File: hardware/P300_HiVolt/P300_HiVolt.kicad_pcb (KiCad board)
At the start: 2 copper layers, 14 parts, among them J1 Conn_01x02, J2 Conn_01x08, J3 Conn_01x06, J4 Conn_01x06, J5 12V, J6 5V, T1 HLK-PM12, T2 HLK-PM05

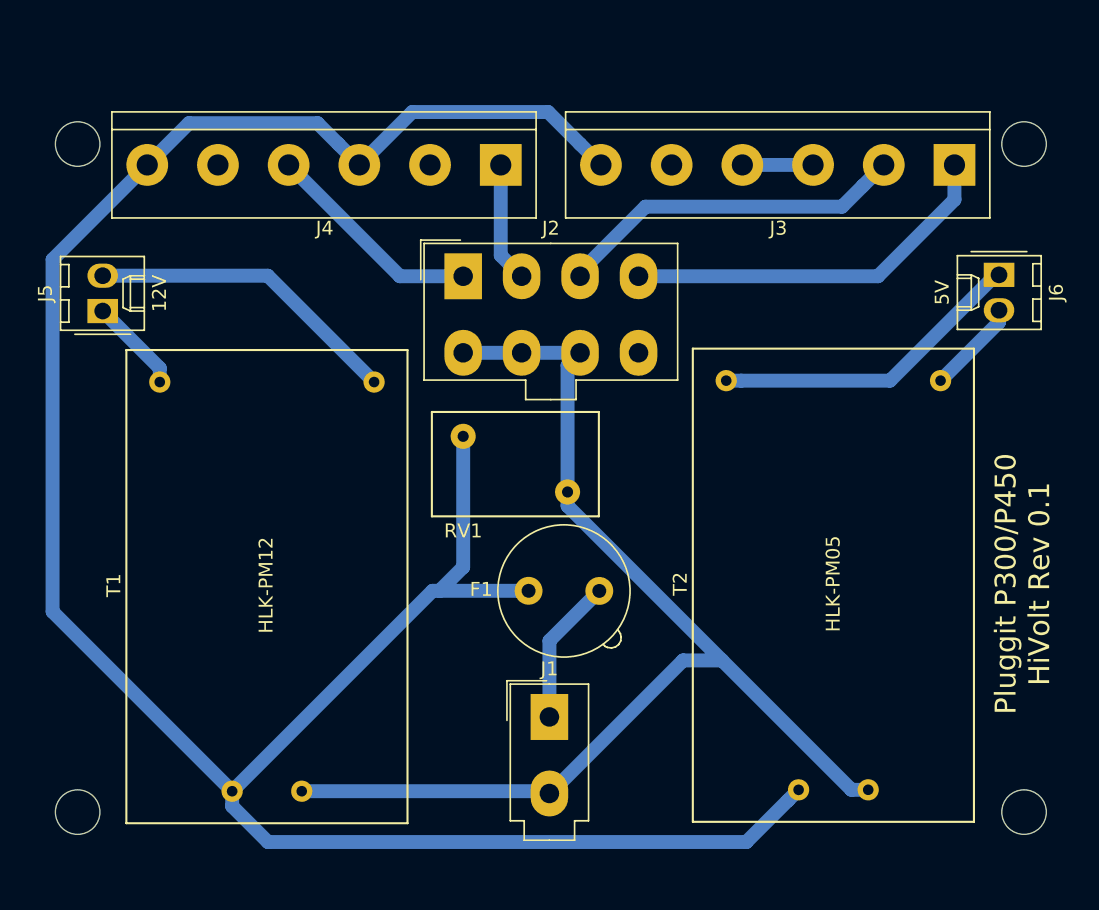
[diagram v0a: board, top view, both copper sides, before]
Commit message: Update der Platinen auf 0.23-dev
Änderungen von 0.22 zu 0.23 - P300_Arduino_IF
 - Linke Seite der Platine vergrößert auf ArduinoMega-Größe
 - Stecker für Displayanschluß ergänzt
 - Fünf weitere Bohrungen für Befestigung ergänzt
 - Leiterbahnen im größeren Abstand zu Durchbohrungen und Bauteilen verlegt
 - Connector für J12 I2C nach links verschoben, damit ausreichend Platz für JTS Stecker
 - Auf dem Stecker J4 sind die beiden Lüfteranschlüsse Lüfter 1 und Lüfter 2 getauscht. Damit ist der Stecker kompatibel zu Pluggit. Der Pluggit-Lüfter-Steuerstecker kann direkt aufgesteckt werden, wenn Molex Stiftleiste - KK - 1x8-polig - Stecker, Molex-Best-Nr. 22272081 verwendet wird.

Änderungen von 0.22 zu 0.23 - P300_HiVolt
 - 230V Lüfteranschluss kompatibel zu Pluggit, Molex Stiftleiste - Mini-Fit Jr - 2x4-polig - Stecker, Molex-Best-Nr. 39281083
 - Stecker J3, J4 für Relais auf Molex Stiftleiste - Mini-Fit Jr - 2x3-polig - Stecker, Molex-Best-Nr. 39288060 geändert.
 - Änderung der Belegung der Stecker J3, J4 für die Verwendung es Relaisboards mit den Ralaisanschlüssen: Mitte = Stromzuführung, links = Nicht geschaltet, rechts geschaltet
 - Räumliche Trennung von 230V und Niedervoltspannungen auf der Platine
 
Neu 0.23 - P300_Display_IF
 - Platine zum Aufstecken des Displays für die räumlich getrennte Montage von Display zu P300_Arduino_IF
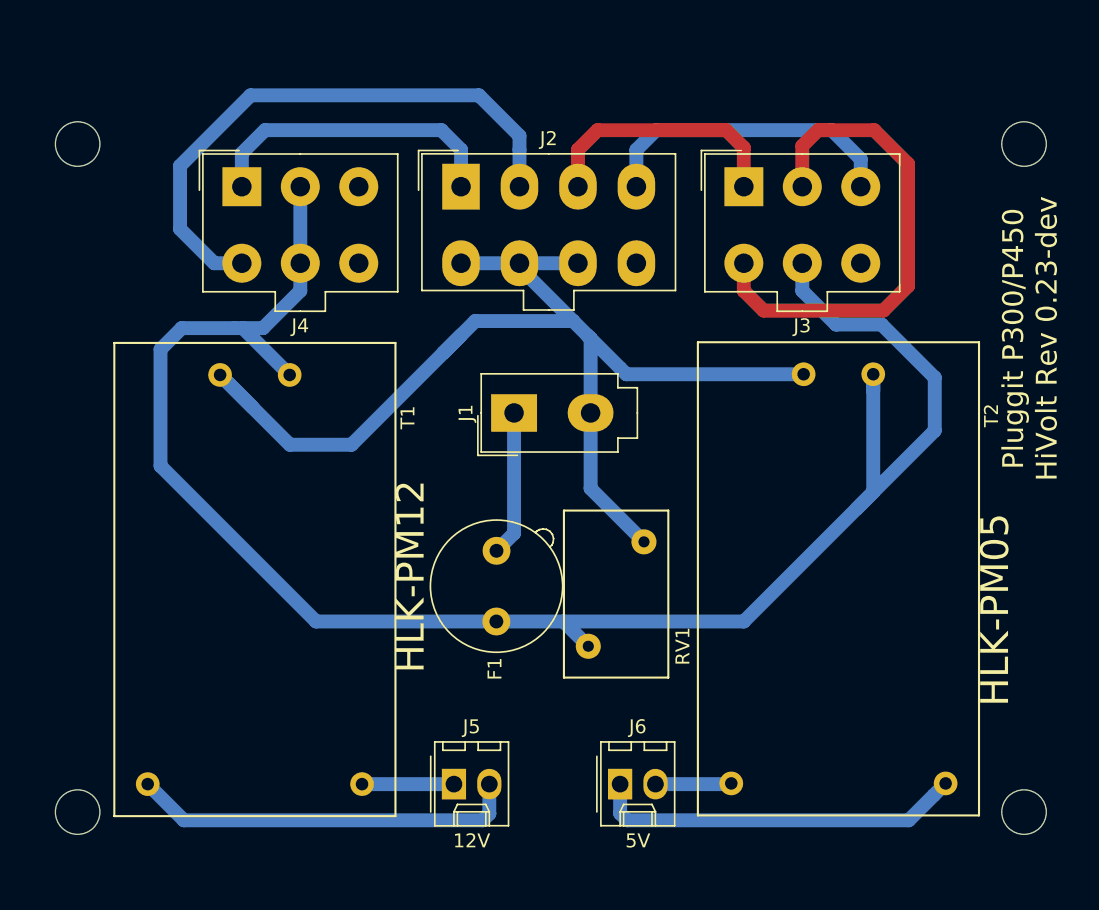
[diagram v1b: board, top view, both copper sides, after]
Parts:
- J3, J4: value Conn_01x06 -> Stiftleiste 6P - Molex; footprint TerminalBlock:TerminalBlock_bornier-6_P5.08mm -> Connectors_Molex:Molex_MiniFit-JR-5556-06A_2x03x4.20mm_Straight
- moved J6 45.6 mm to (125.5, 110.5), turned to 0 degrees
- moved J5 42.3 mm to (113.5, 110.5), turned to 0 degrees
- moved T1 40.4 mm to (89.1, 78.8), turned to 270 degrees
- moved T2 39.8 mm to (131.1, 78.7), turned to 270 degrees
- moved J1 22.0 mm to (117.9, 83.8), turned to 90 degrees
- moved J4 18.7 mm to (98.3, 67.6), turned to 0 degrees
- moved RV1 17.6 mm to (123.2, 100.6), turned to 90 degrees
- moved J3 15.2 mm to (134.4, 67.6), turned to 0 degrees
- moved J2 6.44 mm to (114.0, 67.6)
- moved F1 3.20 mm to (116.6, 98.8), turned to 90 degrees
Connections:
- J2 pad 1: L1_L -> L2_L
- J2 pad 2: L2_L -> L1_L
- J3 pad 1: BP_Z -> BP_A
- J3 pad 2: BP_A -> Net-(J3-Pad2)
- J3 pad 3: Net-(J3-Pad3) -> BP_Z
- J3 pad 4: Net-(J3-Pad3) -> Net-(J3-Pad2)
- J3 pad 5: Net-(J3-Pad5) -> L
- J3 pad 6: L -> Net-(J3-Pad6)
- J4 pad 2: Net-(J4-Pad2) -> L
- J4 pad 3: L -> Net-(J4-Pad3)
- J4 pad 5: Net-(J4-Pad5) -> L
- J4 pad 6: L -> Net-(J4-Pad6)
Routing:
- net L: track 186.0 -> 140.5 mm
- net Net-(J3-Pad2): track 0.00 -> 35.9 mm
- net L1_L: track 15.9 -> 41.3 mm
- net L2_L: track 8.62 -> 22.1 mm
- net BP_A: track 25.3 -> 19.4 mm
- net /V+: track 22.7 -> 27.9 mm
- net BP_Z: track 27.5 -> 22.2 mm
- net Net-(J3-Pad3): track 5.08 -> 0.00 mm
- net /5V-: track 22.7 -> 26.8 mm
- net /5V+: track 6.80 -> 5.47 mm
- net N: track 84.5 -> 85.1 mm
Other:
- net class Power: clearance 1 -> 1.5
- rule trace_min: 0.2 -> 1
- board text added: "Pluggit P300/P450 HiVolt Rev 0.23-dev"
- board text removed: "Pluggit P300/P450 HiVolt Rev 0.1"

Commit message: Platinen V.23 in die Herstellung gegeben
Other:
- board text added: "Pluggit P300/P450 HiVolt Rev 0.23"
- board text removed: "Pluggit P300/P450 HiVolt Rev 0.23-dev"
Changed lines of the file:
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@@
-(kicad_pcb (version 20171130) (host pcbnew "(5.0.2)-1")
+(kicad_pcb (version 20171130) (host pcbnew "(5.0.1)-3")
   (general
     (thickness 1.6)
@@
     (mod_text_size 1 1)
     (mod_text_width 0.15)
-    (pad_size 1.7 1.7)
-    (pad_drill 0.9)
+    (pad_size 1.8 1.8)
+    (pad_drill 1)
     (pad_to_mask_clearance 0.2)
     (solder_mask_min_width 0.25)
@@
     (visible_elements 7FFFFFFF)
     (pcbplotparams
-      (layerselection 0x010fc_ffffffff)
+      (layerselection 0x010f0_ffffffff)
       (usegerberextensions true)
       (usegerberattributes false)
@@
     (fp_line (start 9.75 -1.75) (end 9.75 5.75) (layer F.Fab) (width 0.1))
     (fp_line (start -2.25 -1.75) (end -2.25 5.75) (layer F.Fab) (width 0.1))
-    (pad 1 thru_hole circle (at 0 0 90) (size 1.8 1.8) (drill 0.8) (layers *.Cu *.Mask)
+    (pad 1 thru_hole circle (at 0 0 90) (size 1.8 1.8) (drill 1) (layers *.Cu *.Mask)
       (net 3 L))
-    (pad 2 thru_hole circle (at 7.5 4 90) (size 1.8 1.8) (drill 0.8) (layers *.Cu *.Mask)
+    (pad 2 thru_hole circle (at 7.5 4 90) (size 1.8 1.8) (drill 1) (layers *.Cu *.Mask)
       (net 4 N))
     (model ${KISYS3DMOD}/Varistor.3dshapes/RV_Disc_D12mm_W7.5mm_P7.5mm.wrl
@@
     (arrow2b (pts (xy 76 115.699512) (xy 75.413579 114.573008)))
   )
-  (gr_text "Pluggit P300/P450\nHiVolt Rev 0.23-dev" (at 154.94 78.486 90) (layer F.SilkS)
+  (gr_text "Pluggit P300/P450\nHiVolt Rev 0.23" (at 154.94 78.486 90) (layer F.SilkS)
     (effects (font (size 1.5 1.5) (thickness 0.3)))
   )

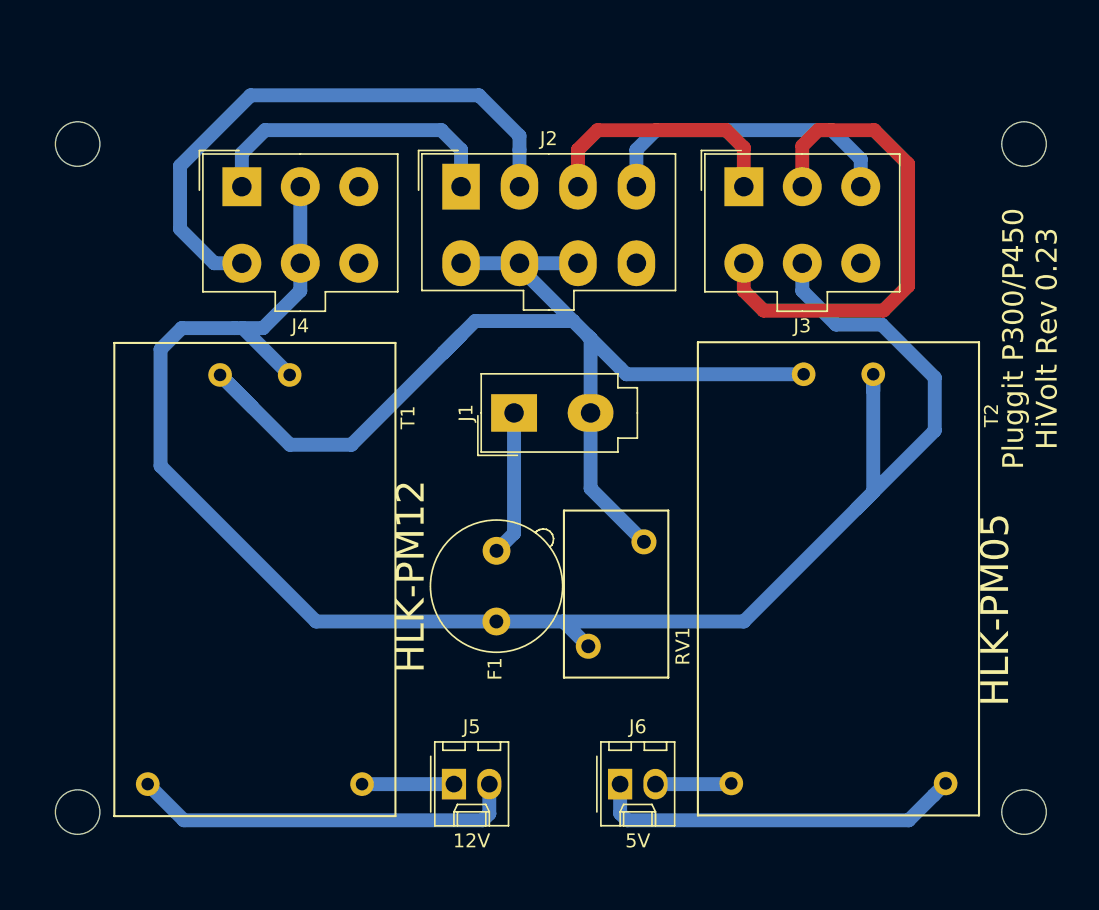
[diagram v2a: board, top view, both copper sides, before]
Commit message: Update  P300_HiVolt Platine
 - Anschluss zu Relais per Schraubklemmen, anstatt Molex Stecker, wegen der schwierigen Beschaffung und Crimpen der Molex Verbindung
 - Alternative für 5V Spannung Meanwell IRM-05-5 mit 5W(1A) Leistung hinzugefügt, empfohlen bei Verwendung Display
 - Platine 3mm verlängert
 - Bohr in Mitte/unten hinzugefügt
 - Leiterbahnen zu den Lüftern auf 2mm verbreitert
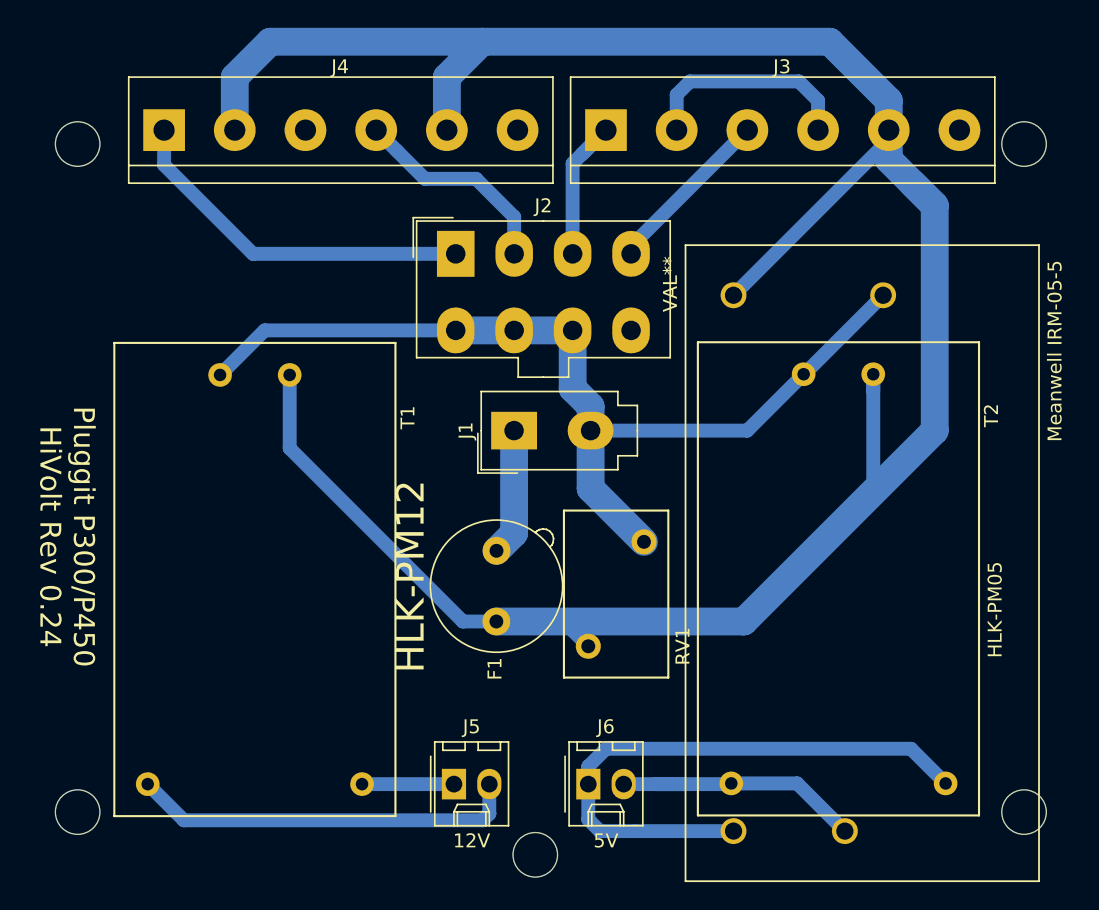
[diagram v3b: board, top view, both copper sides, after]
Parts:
- added ?: MountingHole_3.2mm_M3, Mounting_Holes:MountingHole_3.2mm_M3, F.Cu at (119.4, 115.6)
- added Meanwell IRM-05-5: VAL**, IRM-05-5:CONV_IRM-05-5, F.Cu at (142.9, 94.6)
- J3, J4: value Stiftleiste 6P - Molex -> Stiftleiste 6P; footprint Connectors_Molex:Molex_MiniFit-JR-5556-06A_2x03x4.20mm_Straight -> Connectors_Terminal_Blocks:TerminalBlock_bornier-6_P5.08mm
- moved J3 10.7 mm to (124.5, 63.5)
- moved J4 6.91 mm to (92.7, 63.5)
- moved J2 4.84 mm to (113.7, 72.4)
- moved J6 2.29 mm to (123.2, 110.5)
- moved J1 1.27 mm to (117.9, 85.1)
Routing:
- net L: track 140.5 -> 229.9 mm
- net L1_L: track 41.3 -> 15.4 mm
- net Net-(J3-Pad2): track 35.9 -> 15.8 mm
- net /5V+: track 5.47 -> 19.4 mm
- net BP_Z: track 22.2 -> 12.4 mm
- net /5V-: track 26.8 -> 34.8 mm
- net N: track 85.1 -> 77.7 mm
- net BP_A: track 19.4 -> 12.4 mm
- net (no net): track 0.00 -> 7.06 mm
- net L2_L: track 22.1 -> 26.1 mm
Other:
- net class Default: trace_width 0.25 -> 1
- board text added: "Pluggit P300/P450 HiVolt Rev 0.24"
- board text removed: "Pluggit P300/P450 HiVolt Rev 0.23"
